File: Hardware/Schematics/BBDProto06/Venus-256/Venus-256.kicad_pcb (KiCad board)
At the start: 2 copper layers, 172.7 x 109.2 mm, 225 parts, among them J201 RaspberryPi header, J301 ARM JTAG, U1001 AD7616, U101 TPS22993, U401 AD7616, U501 ATSAME70Q21A-AN, U601 AD7616, U701 AD7616, U801 AD7616, U901 ATSAME70Q21A-AN

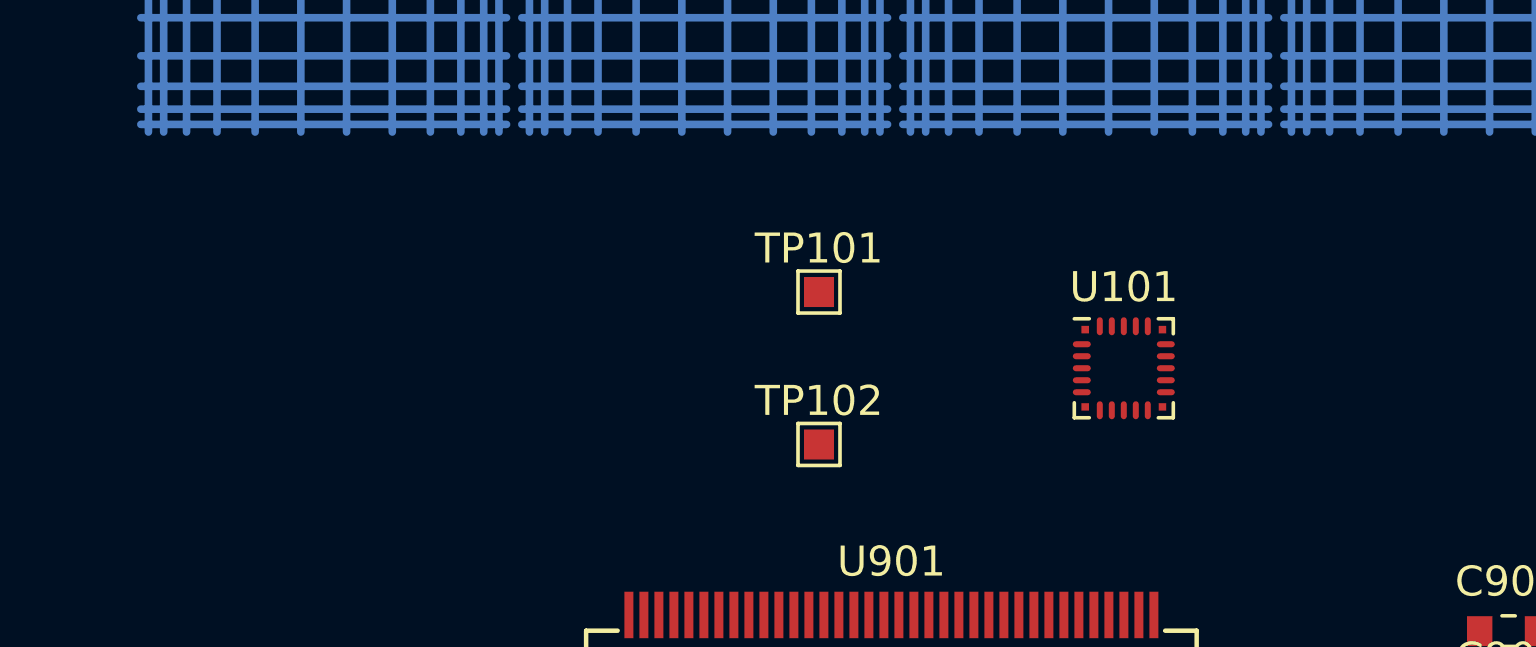
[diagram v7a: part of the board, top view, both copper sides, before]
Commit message: Added jumpers to TPS22993
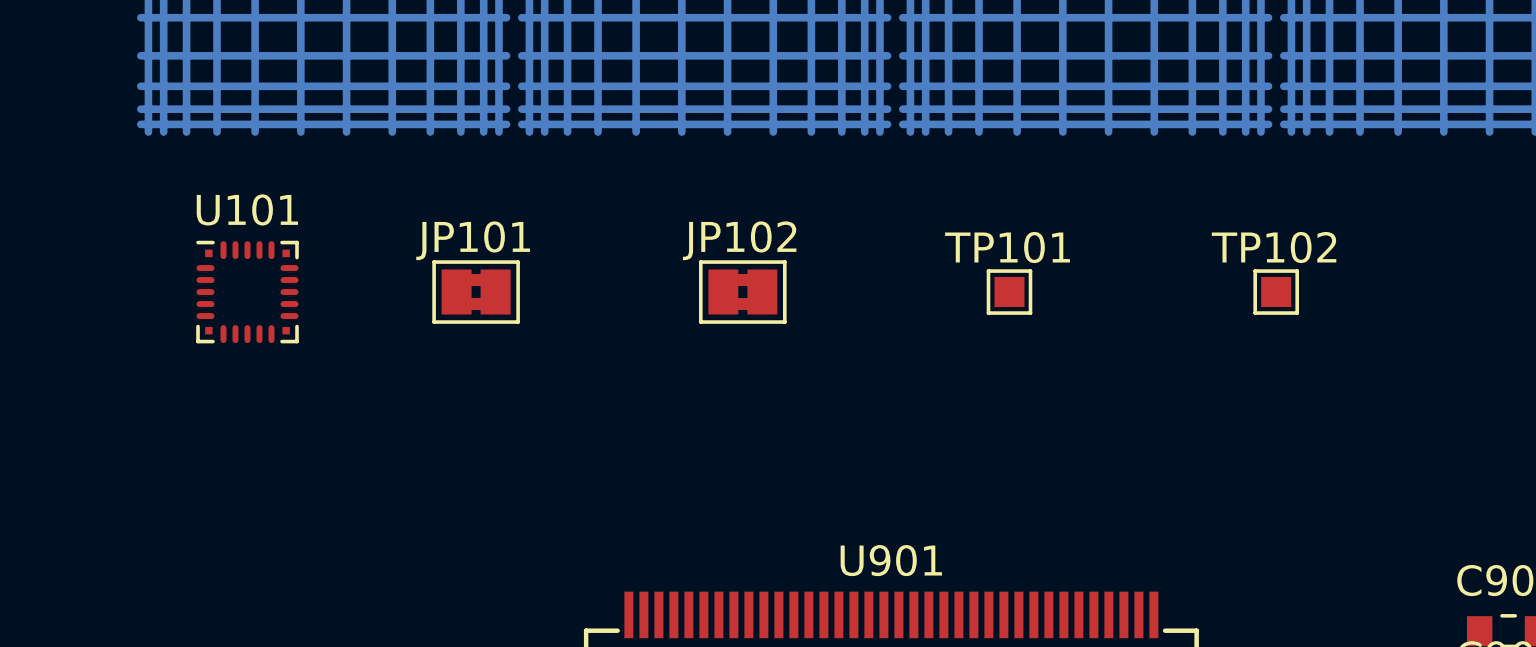
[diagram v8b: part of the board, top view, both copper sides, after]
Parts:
- added JP101: VOUT1_JP, Jumper:SolderJumper-2_P1.3mm_Bridged2Bar_Pad1.0x1.5mm, F.Cu at (31.8, 76.2)
- added JP102: VOUT2_JP, Jumper:SolderJumper-2_P1.3mm_Bridged2Bar_Pad1.0x1.5mm, F.Cu at (40.6, 76.2)
- moved U101 29.3 mm to (24.1, 76.2)
- moved TP102 16.1 mm to (58.4, 76.2)
- moved TP101 6.35 mm to (49.5, 76.2)
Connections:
- U101 pad 1: /CellMaster-02/VCC_MCU_P3V3 -> Net-(JP102-Pad1)
- U101 pad 5: /CellMaster-01/VCC_MCU_P3V3 -> Net-(JP101-Pad1)
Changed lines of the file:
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@@
     (tracks 9412)
     (zones 0)
-    (modules 225)
-    (nets 161)
+    (modules 227)
+    (nets 163)
   )
   (page A4)
@@
   (net 159 "Net-(TP817-Pad1)")
   (net 160 "Net-(TP1017-Pad1)")
+  (net 161 "Net-(JP102-Pad1)")
+  (net 162 "Net-(JP101-Pad1)")
   (net_class Default "This is the default net class."
     (clearance 0.254)
@@
     (add_net "Net-(J301-Pad7)")
     (add_net "Net-(J301-Pad9)")
+    (add_net "Net-(JP101-Pad1)")
+    (add_net "Net-(JP102-Pad1)")
     (add_net "Net-(TP1002-Pad1)")
     (add_net "Net-(TP1003-Pad1)")
@@
   )
   (module TestPoint:TestPoint_Pad_1.0x1.0mm (layer F.Cu)
-    (at 43.18 76.2)
+    (at 49.53 76.2)
     (descr "SMD rectangular pad as test Point, square 1.0mm side length")
     (tags "test point SMD pad rectangle square")
@@
   )
   (module TestPoint:TestPoint_Pad_1.0x1.0mm (layer F.Cu)
-    (at 43.18 81.28)
+    (at 58.42 76.2)
     (descr "SMD rectangular pad as test Point, square 1.0mm side length")
     (tags "test point SMD pad rectangle square")
@@
   )
   (module Package_DFN_QFN:Texas_S-PWQFN-N20 (layer F.Cu)
-    (at 53.34 78.74)
+    (at 24.13 76.2)
     (descr "20-Pin Plastic Quad Flatpack No-Lead Package, Body 3.0x3.0x0.8mm, Texas Instruments (http://www.ti.com/lit/ds/symlink/tps22993.pdf)")
     (tags "QFN 0.4")
@@
     (fp_line (start -1.95 1.95) (end -1.95 -1.95) (layer F.CrtYd) (width 0.05))
     (pad 1 smd oval (at -1.4 -0.8 90) (size 0.2 0.6) (layers F.Cu F.Paste F.Mask)
-      (net 5 /CellMaster-02/VCC_MCU_P3V3))
+      (net 161 "Net-(JP102-Pad1)"))
     (pad 2 smd oval (at -1.4 -0.4 90) (size 0.2 0.6) (layers F.Cu F.Paste F.Mask)
       (net 3 /RaspberryPiGPIOHeader/DC_POWER_3V3))
@@
       (net 3 /RaspberryPiGPIOHeader/DC_POWER_3V3))
     (pad 5 smd oval (at -1.4 0.8 90) (size 0.2 0.6) (layers F.Cu F.Paste F.Mask)
-      (net 4 /CellMaster-01/VCC_MCU_P3V3))
+      (net 162 "Net-(JP101-Pad1)"))
     (pad 6 smd oval (at -0.8 1.4) (size 0.2 0.6) (layers F.Cu F.Paste F.Mask)
       (net 1 GND))
@@
     )
   )
+  (module Jumper:SolderJumper-2_P1.3mm_Bridged2Bar_Pad1.0x1.5mm (layer F.Cu)
+    (at 31.75 76.2)
+    (descr "SMD Solder Jumper, 1x1.5mm Pads, 0.3mm gap, bridged with 2 copper strips")
+    (tags "solder jumper open")
+    (attr virtual)
+    (fp_text reference JP101 (at 0 -1.8) (layer F.SilkS)
+      (effects (font (size 1 1) (thickness 0.15)))
+    )
+    (fp_text value VOUT1_JP (at 0 1.9) (layer F.Fab)
+      (effects (font (size 1 1) (thickness 0.15)))
+    )
+    (fp_line (start -1.4 1) (end -1.4 -1) (layer F.SilkS) (width 0.12))
+    (fp_line (start 1.4 1) (end -1.4 1) (layer F.SilkS) (width 0.12))
+    (fp_line (start 1.4 -1) (end 1.4 1) (layer F.SilkS) (width 0.12))
+    (fp_line (start -1.4 -1) (end 1.4 -1) (layer F.SilkS) (width 0.12))
+    (fp_line (start -1.65 -1.25) (end 1.65 -1.25) (layer F.CrtYd) (width 0.05))
+    (fp_line (start -1.65 -1.25) (end -1.65 1.25) (layer F.CrtYd) (width 0.05))
+    (fp_line (start 1.65 1.25) (end 1.65 -1.25) (layer F.CrtYd) (width 0.05))
+    (fp_line (start 1.65 1.25) (end -1.65 1.25) (layer F.CrtYd) (width 0.05))
+    (pad 1 smd rect (at 0 -0.4) (size 0.5 0.4) (layers F.Cu F.Mask)
+      (net 162 "Net-(JP101-Pad1)"))
+    (pad 1 smd rect (at 0 0.4) (size 0.5 0.4) (layers F.Cu F.Mask)
+      (net 162 "Net-(JP101-Pad1)"))
+    (pad 2 smd rect (at 0.65 0) (size 1 1.5) (layers F.Cu F.Mask)
+      (net 4 /CellMaster-01/VCC_MCU_P3V3))
+    (pad 1 smd rect (at -0.65 0) (size 1 1.5) (layers F.Cu F.Mask)
+      (net 162 "Net-(JP101-Pad1)"))
+  )
+  (module Jumper:SolderJumper-2_P1.3mm_Bridged2Bar_Pad1.0x1.5mm (layer F.Cu)
+    (at 40.64 76.2)
+    (descr "SMD Solder Jumper, 1x1.5mm Pads, 0.3mm gap, bridged with 2 copper strips")
+    (tags "solder jumper open")
+    (attr virtual)
+    (fp_text reference JP102 (at 0 -1.8) (layer F.SilkS)
+      (effects (font (size 1 1) (thickness 0.15)))
+    )
+    (fp_text value VOUT2_JP (at 0 1.9) (layer F.Fab)
+      (effects (font (size 1 1) (thickness 0.15)))
+    )
+    (fp_line (start 1.65 1.25) (end -1.65 1.25) (layer F.CrtYd) (width 0.05))
+    (fp_line (start 1.65 1.25) (end 1.65 -1.25) (layer F.CrtYd) (width 0.05))
+    (fp_line (start -1.65 -1.25) (end -1.65 1.25) (layer F.CrtYd) (width 0.05))
+    (fp_line (start -1.65 -1.25) (end 1.65 -1.25) (layer F.CrtYd) (width 0.05))
+    (fp_line (start -1.4 -1) (end 1.4 -1) (layer F.SilkS) (width 0.12))
+    (fp_line (start 1.4 -1) (end 1.4 1) (layer F.SilkS) (width 0.12))
+    (fp_line (start 1.4 1) (end -1.4 1) (layer F.SilkS) (width 0.12))
+    (fp_line (start -1.4 1) (end -1.4 -1) (layer F.SilkS) (width 0.12))
+    (pad 1 smd rect (at -0.65 0) (size 1 1.5) (layers F.Cu F.Mask)
+      (net 161 "Net-(JP102-Pad1)"))
+    (pad 2 smd rect (at 0.65 0) (size 1 1.5) (layers F.Cu F.Mask)
+      (net 5 /CellMaster-02/VCC_MCU_P3V3))
+    (pad 1 smd rect (at 0 0.4) (size 0.5 0.4) (layers F.Cu F.Mask)
+      (net 161 "Net-(JP102-Pad1)"))
+    (pad 1 smd rect (at 0 -0.4) (size 0.5 0.4) (layers F.Cu F.Mask)
+      (net 161 "Net-(JP102-Pad1)"))
+  )
   (dimension 172.72 (width 0.3) (layer Dwgs.User)
